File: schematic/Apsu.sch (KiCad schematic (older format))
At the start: 28 parts

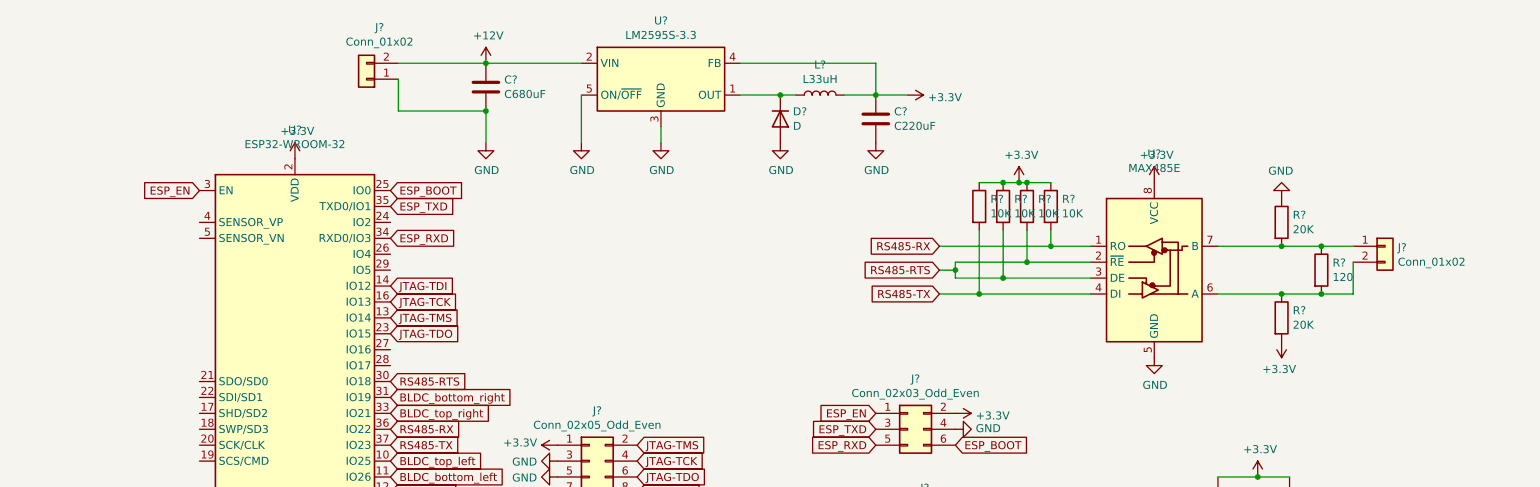
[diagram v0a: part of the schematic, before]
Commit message: more connectors
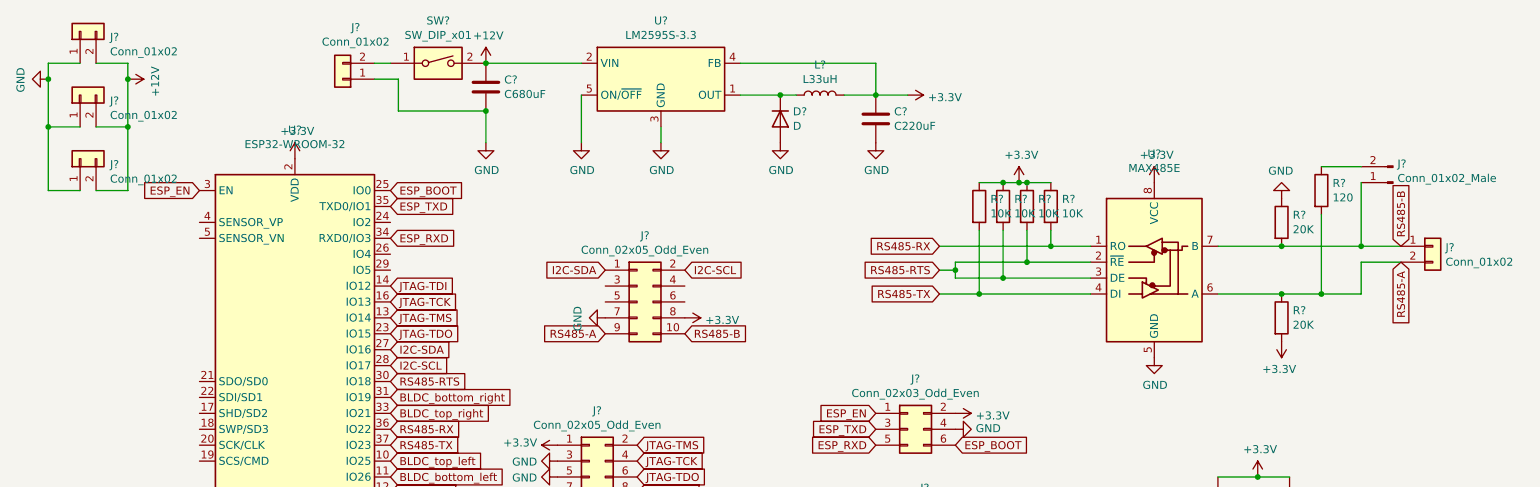
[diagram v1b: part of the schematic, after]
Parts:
- added J? (x3): Conn_01x02, symbol Connector_Generic:Conn_01x02
- added J?: Conn_02x05_Odd_Even, symbol Connector_Generic:Conn_02x05_Odd_Even
- added J?: Conn_01x02_Male, symbol Connector:Conn_01x02_Male
- added SW?: SW_DIP_x01, symbol Switch:SW_DIP_x01
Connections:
- net +12V: now also J?.2 (Pin_2), J?.2 (Pin_2), J?.2 (Pin_2), SW?.2; no longer J?.2 (Pin_2)
- net +3V3: now also J?.8 (Pin_8)
- net GND: now also J?.1 (Pin_1), J?.1 (Pin_1), J?.1 (Pin_1), J?.7 (Pin_7)
- net I2C-SDA: now reaches U?.27 (IO16)
- net I2C-SDA: now also J?.1 (Pin_1)
- net I2C-SCL: now reaches U?.28 (IO17)
- net I2C-SCL: now also J?.2 (Pin_2)
- net RS485-B: now reaches J?.1 (Pin_1), R?.2, U?.7 (B)
- net RS485-B: now also J?.1 (Pin_1), J?.10 (Pin_10); no longer R?.1
- net RS485-A: now reaches J?.2 (Pin_2), R?.1, R?.2, U?.6 (A)
- net RS485-A: now also J?.9 (Pin_9)
- new net: J?.2 (Pin_2), SW?.1
- new net: J?.2 (Pin_2), R?.1
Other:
- moved on the sheet: J?, R?
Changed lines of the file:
@@
 $EndDescr
-$Comp
-L RF_Module:ESP32-WROOM-32 U?
-U 1 1 5EBF8AC7
-P 2400 2950
-F 0 "U?" H 2400 4531 50  0000 C CNN
-F 1 "ESP32-WROOM-32" H 2400 4440 50  0000 C CNN
-F 2 "RF_Module:ESP32-WROOM-32" H 2400 1450 50  0001 C CNN
-F 3 "https://www.espressif.com/sites/default/files/documentation/esp32-wroom-32_datasheet_en.pdf" H 2100 3000 50  0001 C CNN
-	1    2400 2950
-	1    0    0    -1
-$EndComp
 $Comp
 L Regulator_Switching:LM2595S-3.3 U?
@@
 	1    0    0    -1
 $EndComp
-$Comp
-L Connector_Generic:Conn_01x02 J?
-U 1 1 5EC3CD88
-P 2850 1050
-F 0 "J?" H 2768 725 50  0000 C CNN
-F 1 "Conn_01x02" H 2768 816 50  0000 C CNN
-F 2 "" H 2850 1050 50  0001 C CNN
-F 3 "~" H 2850 1050 50  0001 C CNN
-	1    2850 1050
-	-1   0    0    1
-$EndComp
-Wire Wire Line
-	3050 950  3600 950
 Wire Wire Line
 	3050 1050 3050 1250
@@
 L Connector_Generic:Conn_01x02 J?
 U 1 1 5EC453EB
-P 9250 2100
-F 0 "J?" H 9330 2092 50  0000 L CNN
-F 1 "Conn_01x02" H 9330 2001 50  0000 L CNN
-F 2 "" H 9250 2100 50  0001 C CNN
-F 3 "~" H 9250 2100 50  0001 C CNN
-	1    9250 2100
+P 9550 2100
+F 0 "J?" H 9630 2092 50  0000 L CNN
+F 1 "Conn_01x02" H 9630 2001 50  0000 L CNN
+F 2 "" H 9550 2100 50  0001 C CNN
+F 3 "~" H 9550 2100 50  0001 C CNN
+	1    9550 2100
 	1    0    0    -1
 $EndComp
@@
 Wire Wire Line
 	8200 2400 8600 2400
-Wire Wire Line
-	8600 2100 8850 2100
 Connection ~ 8600 2100
-Wire Wire Line
-	8600 2400 8850 2400
-Wire Wire Line
-	9050 2400 9050 2200
 Connection ~ 8600 2400
 $Comp
 L Device:R R?
 U 1 1 5EC55FF9
-P 8850 2250
-F 0 "R?" H 8920 2296 50  0000 L CNN
-F 1 "120" H 8920 2205 50  0000 L CNN
-F 2 "" V 8780 2250 50  0001 C CNN
-F 3 "~" H 8850 2250 50  0001 C CNN
-	1    8850 2250
-	1    0    0    -1
-$EndComp
-Connection ~ 8850 2100
-Wire Wire Line
-	8850 2100 9050 2100
-Connection ~ 8850 2400
-Wire Wire Line
-	8850 2400 9050 2400
+P 8850 1750
+F 0 "R?" H 8920 1796 50  0000 L CNN
+F 1 "120" H 8920 1705 50  0000 L CNN
+F 2 "" V 8780 1750 50  0001 C CNN
+F 3 "~" H 8850 1750 50  0001 C CNN
+	1    8850 1750
+	1    0    0    -1
+$EndComp
 Text GLabel 6450 2100 0    50   Input ~ 0
 RS485-RX
@@
 	4950 4850 4950 4650
 Connection ~ 4500 4850
+$Comp
+L RF_Module:ESP32-WROOM-32 U?
+U 1 1 5EBF8AC7
+P 2400 2950
+F 0 "U?" H 2400 4531 50  0000 C CNN
+F 1 "ESP32-WROOM-32" H 2400 4440 50  0000 C CNN
+F 2 "RF_Module:ESP32-WROOM-32" H 2400 1450 50  0001 C CNN
+F 3 "https://www.espressif.com/sites/default/files/documentation/esp32-wroom-32_datasheet_en.pdf" H 2100 3000 50  0001 C CNN
+	1    2400 2950
+	1    0    0    -1
+$EndComp
+$Comp
+L Connector_Generic:Conn_01x02 J?
+U 1 1 5ECCDB06
+P 1050 750
+F 0 "J?" V 1014 562 50  0000 R CNN
+F 1 "Conn_01x02" V 923 562 50  0000 R CNN
+F 2 "" H 1050 750 50  0001 C CNN
+F 3 "~" H 1050 750 50  0001 C CNN
+	1    1050 750
+	0    -1   -1   0
+$EndComp
+$Comp
+L Connector_Generic:Conn_01x02 J?
+U 1 1 5ECCDEB5
+P 1050 1150
+F 0 "J?" V 1014 962 50  0000 R CNN
+F 1 "Conn_01x02" V 923 962 50  0000 R CNN
+F 2 "" H 1050 1150 50  0001 C CNN
+F 3 "~" H 1050 1150 50  0001 C CNN
+	1    1050 1150
+	0    -1   -1   0
+$EndComp
+$Comp
+L Connector_Generic:Conn_01x02 J?
+U 1 1 5ECCE19D
+P 1050 1550
+F 0 "J?" V 1014 1362 50  0000 R CNN
+F 1 "Conn_01x02" V 923 1362 50  0000 R CNN
+F 2 "" H 1050 1550 50  0001 C CNN
+F 3 "~" H 1050 1550 50  0001 C CNN
+	1    1050 1550
+	0    -1   -1   0
+$EndComp
+Wire Wire Line
+	1050 1350 850  1350
+Wire Wire Line
+	850  1350 850  1750
+Wire Wire Line
+	850  1750 1050 1750
+Wire Wire Line
+	850  1350 850  1050
+Wire Wire Line
+	850  950  1050 950
+Connection ~ 850  1350
+Wire Wire Line
+	1150 1750 1350 1750
+Wire Wire Line
+	1350 1750 1350 1350
+Wire Wire Line
+	1350 1350 1150 1350
+Wire Wire Line
+	1150 950  1350 950
+Wire Wire Line
+	1350 950  1350 1050
+Connection ~ 1350 1350
+$Comp
+L power:+12V #PWR?
+U 1 1 5ED02DFC
+P 1350 1050
+F 0 "#PWR?" H 1350 900 50  0001 C CNN
+F 1 "+12V" H 1365 1223 50  0000 C CNN
+F 2 "" H 1350 1050 50  0001 C CNN
+F 3 "" H 1350 1050 50  0001 C CNN
+	1    1350 1050
+	0    1    1    0
+$EndComp
+Connection ~ 1350 1050
+Wire Wire Line
+	1350 1050 1350 1350
+$Comp
+L power:GND #PWR?
+U 1 1 5ED036F9
+P 850 1050
+F 0 "#PWR?" H 850 800 50  0001 C CNN
+F 1 "GND" H 855 877 50  0000 C CNN
+F 2 "" H 850 1050 50  0001 C CNN
+F 3 "" H 850 1050 50  0001 C CNN
+	1    850  1050
+	0    1    1    0
+$EndComp
+Connection ~ 850  1050
+Wire Wire Line
+	850  1050 850  950
+$Comp
+L Connector_Generic:Conn_01x02 J?
+U 1 1 5EC3CD88
+P 2700 1050
+F 0 "J?" H 2618 725 50  0000 C CNN
+F 1 "Conn_01x02" H 2618 816 50  0000 C CNN
+F 2 "" H 2700 1050 50  0001 C CNN
+F 3 "~" H 2700 1050 50  0001 C CNN
+	1    2700 1050
+	-1   0    0    1
+$EndComp
+$Comp
+L Switch:SW_DIP_x01 SW?
+U 1 1 5ED13974
+P 3300 950
+F 0 "SW?" H 3300 1217 50  0000 C CNN
+F 1 "SW_DIP_x01" H 3300 1126 50  0000 C CNN
+F 2 "" H 3300 950 50  0001 C CNN
+F 3 "~" H 3300 950 50  0001 C CNN
+	1    3300 950
+	1    0    0    -1
+$EndComp
+Wire Wire Line
+	3000 950  2900 950
+Wire Wire Line
+	2900 1050 3050 1050
+$Comp
+L Connector_Generic:Conn_02x05_Odd_Even J?
+U 1 1 5ED317E1
+P 4550 2450
+F 0 "J?" H 4600 2867 50  0000 C CNN
+F 1 "Conn_02x05_Odd_Even" H 4600 2776 50  0000 C CNN
+F 2 "" H 4550 2450 50  0001 C CNN
+F 3 "~" H 4550 2450 50  0001 C CNN
+	1    4550 2450
+	1    0    0    -1
+$EndComp
+Text GLabel 3000 2750 2    50   Input ~ 0
+I2C-SDA
+Text GLabel 3000 2850 2    50   Input ~ 0
+I2C-SCL
+Text GLabel 4350 2250 0    50   Input ~ 0
+I2C-SDA
+Text GLabel 4850 2250 2    50   Input ~ 0
+I2C-SCL
+$Comp
+L power:GND #PWR?
+U 1 1 5ED5B109
+P 4350 2550
+F 0 "#PWR?" H 4350 2300 50  0001 C CNN
+F 1 "GND" H 4355 2377 50  0000 C CNN
+F 2 "" H 4350 2550 50  0001 C CNN
+F 3 "" H 4350 2550 50  0001 C CNN
+	1    4350 2550
+	0    1    1    0
+$EndComp
+$Comp
+L power:+3.3V #PWR?
+U 1 1 5ED5B8B2
+P 4850 2550
+F 0 "#PWR?" H 4850 2400 50  0001 C CNN
+F 1 "+3.3V" V 4865 2678 50  0000 L CNN
+F 2 "" H 4850 2550 50  0001 C CNN
+F 3 "" H 4850 2550 50  0001 C CNN
+	1    4850 2550
+	0    1    1    0
+$EndComp
+$Comp
+L Connector:Conn_01x02_Male J?
+U 1 1 5ED63CAE
+P 9300 1700
+F 0 "J?" H 9272 1582 50  0000 R CNN
+F 1 "Conn_01x02_Male" H 9272 1673 50  0000 R CNN
+F 2 "" H 9300 1700 50  0001 C CNN
+F 3 "~" H 9300 1700 50  0001 C CNN
+	1    9300 1700
+	-1   0    0    1
+$EndComp
+Wire Wire Line
+	9100 1600 8850 1600
+Wire Wire Line
+	9100 1700 9100 2100
+Connection ~ 9100 2100
+Wire Wire Line
+	9100 2200 9100 2400
+Wire Wire Line
+	8600 2400 8850 2400
+Wire Wire Line
+	8600 2100 9100 2100
+Wire Wire Line
+	8850 1900 8850 2400
+Connection ~ 8850 2400
+Wire Wire Line
+	8850 2400 9100 2400
+Text GLabel 9350 2200 3    50   Input ~ 0
+RS485-A
+Text GLabel 9350 2100 1    50   Input ~ 0
+RS485-B
+Wire Wire Line
+	9100 2100 9350 2100
+Wire Wire Line
+	9100 2200 9350 2200
+Text GLabel 4350 2650 0    50   Input ~ 0
+RS485-A
+Text GLabel 4850 2650 2    50   Input ~ 0
+RS485-B
 $EndSCHEMATC

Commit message: dingentjes
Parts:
- added J? (x2): Conn_01x04_Male, symbol Connector:Conn_01x04_Male
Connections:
- net GND: now also J?.1 (Pin_1), J?.2 (Pin_2), J?.3 (Pin_3), J?.4 (Pin_4)
- new net +5V: J?.1 (Pin_1), J?.2 (Pin_2), J?.3 (Pin_3), J?.4 (Pin_4)
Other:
- moved on the sheet: C?, J?
